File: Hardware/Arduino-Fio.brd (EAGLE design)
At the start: 27.9 x 64.8 mm, 65 parts, among them U1 MCP73831, U4 XBEE, U5 ATMEGA32U4, U6 MIC5219-3.3, X2 USB-MICROB, Y2 8MHz

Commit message: Midway hardware update
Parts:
- X2: value USB-MICROB -> USB_MICROB_PLUGCONN-11752; device SparkFun:USB-MICROB -> SparkFun-Connectors:USB-B-MICRO-SMD_V03
- moved R11 0.32 mm to (7.62, 58.1)
- moved R12 0.32 mm to (8.89, 58.1)
- turned X2 to 270 degrees
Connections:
- removed net N$21: R11.2, X2.D+
- new net N$5: R11.2, X2.D+1
- net GND: now also X2.GND1; no longer X2.GND
- net N$20: now also X2.D-1; no longer X2.D-
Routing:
- net AREF: track 24.8 -> 21.2 mm
- net N$5: track 0.00 -> 1.85 mm
- net N$21: track 1.58 -> 0.00 mm
- net N$1: track 47.2 -> 48.5 mm, vias 1 -> 2
- net GND: track 43.6 -> 42.5 mm, vias 24 -> 27
- net D14: track 47.0 -> 48.1 mm
- net D+: track 43.1 -> 42.4 mm
- net TXO: track 21.9 -> 21.2 mm
- net 3.3V: track 108.5 -> 107.8 mm
- net RST: track 47.4 -> 48.0 mm
- net MOSI: track 38.7 -> 38.2 mm

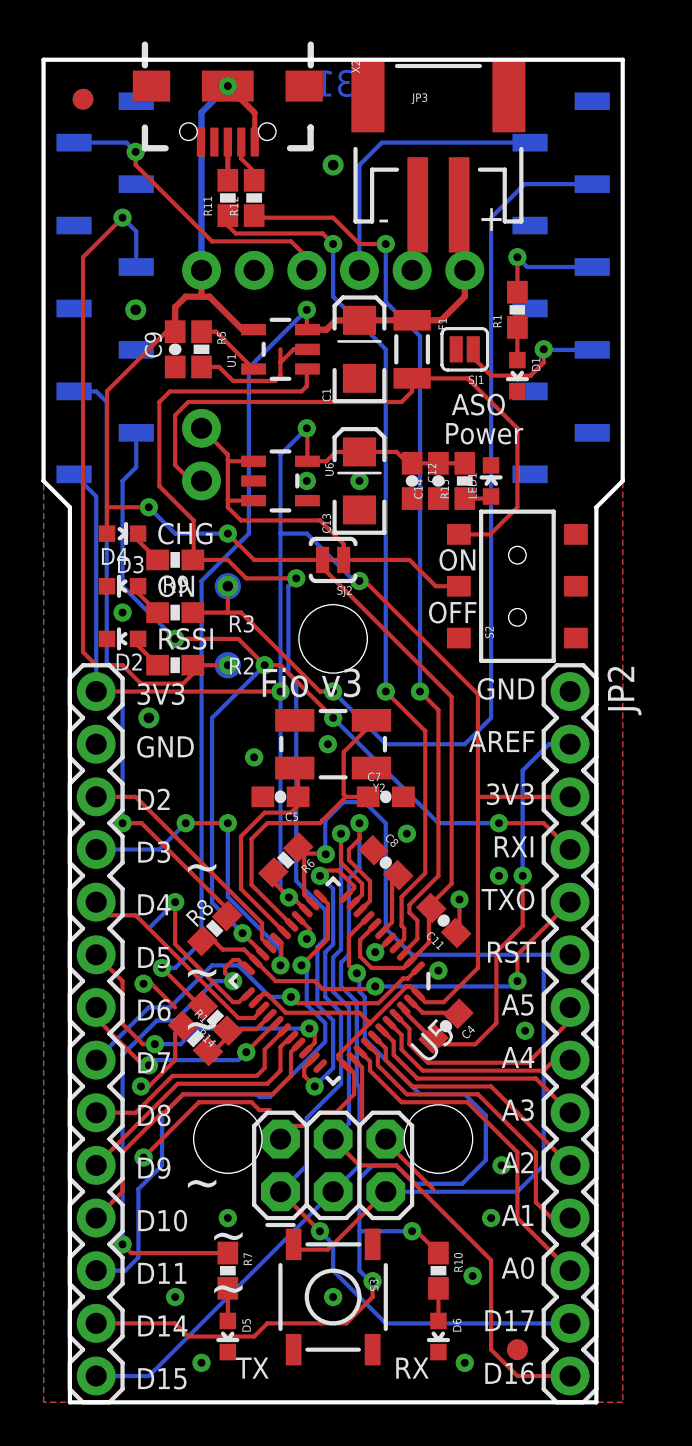
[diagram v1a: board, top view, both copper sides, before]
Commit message: Fixing USB trace issue
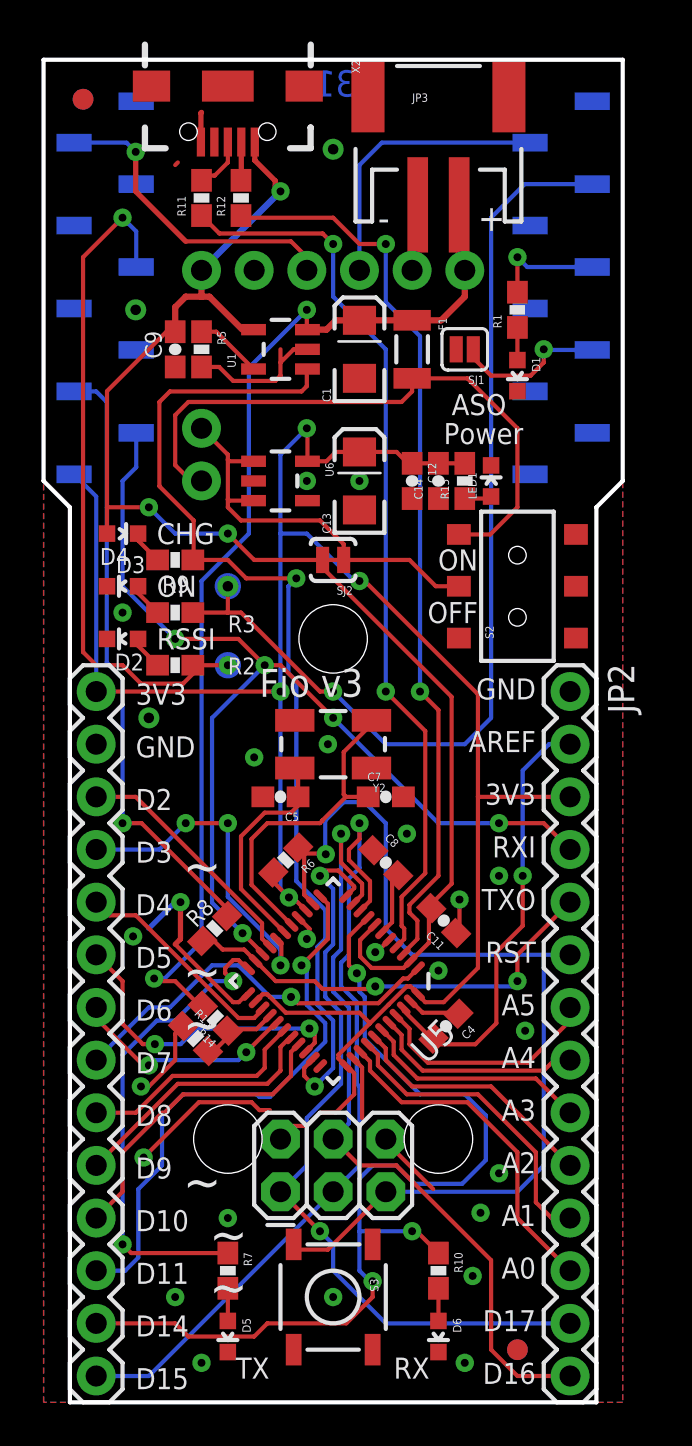
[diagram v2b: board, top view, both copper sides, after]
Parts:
- moved R11 1.27 mm to (6.35, 58.1)
- moved R12 0.63 mm to (8.26, 58.1)
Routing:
- net USB_VCC: track 70.2 -> 65.8 mm
- net D+: track 42.4 -> 43.3 mm
- net N$5: track 1.85 -> 2.61 mm
- net VBATT: track 51.5 -> 52.3 mm
- net SLEEP_RQ: track 14.5 -> 15.3 mm
- net D-: track 43.2 -> 43.9 mm

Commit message: Fixing schematic frame
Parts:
- added U$2: REVISION, SparkFun-Aesthetics:REVISION
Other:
- board text added: "Toni Klopfenstein"
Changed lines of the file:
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@@
 <layer number="47" name="Measures" color="7" fill="1" visible="no" active="yes"/>
 <layer number="48" name="Document" color="7" fill="1" visible="no" active="yes"/>
-<layer number="49" name="Reference" color="7" fill="1" visible="no" active="yes"/>
+<layer number="49" name="Reference" color="7" fill="1" visible="yes" active="yes"/>
 <layer number="50" name="dxf" color="7" fill="1" visible="no" active="yes"/>
 <layer number="51" name="tDocu" color="6" fill="1" visible="yes" active="yes"/>
@@
 <text x="22.479" y="24.765" size="1.016" layer="21" font="vector" ratio="15" rot="R180">TXO</text>
 <text x="22.479" y="22.225" size="1.016" layer="21" font="vector" ratio="15" rot="R180">RST</text>
-<text x="31.75" y="-12.7" size="1.778" layer="27" font="vector" ratio="15">S. Kobayashi and N. Seidle</text>
+<text x="27.94" y="-11.43" size="1.778" layer="27" font="vector" ratio="15">S. Kobayashi and N. Seidle</text>
 <text x="5.715" y="56.261" size="1.27" layer="22" font="vector" ratio="15" rot="MR90">5V</text>
 <text x="9.525" y="55.88" size="1.778" layer="22" font="vector" ratio="15" rot="MR0">-</text>
@@
 <text x="18.034" y="46.228" size="1.016" layer="21" font="vector" ratio="15">Power</text>
 <text x="18.415" y="47.625" size="1.016" layer="21" font="vector" ratio="15">ASO</text>
+<text x="27.94" y="-15.24" size="1.778" layer="27" font="vector" ratio="15">Toni Klopfenstein</text>
 </plain>
 <attributes>
@@
 <element name="FRAME2" library="SparkFun-Aesthetics" package="CREATIVE_COMMONS" value="FRAME-LETTER" x="0.635" y="-11.43"/>
 <element name="LOGO1" library="SparkFun-Aesthetics" package="OSHW-LOGO-L" value="OSHW-LOGOL" x="12.7" y="20.32" rot="MR0"/>
+<element name="U$2" library="SparkFun-Aesthetics" package="REVISION" value="REVISION" x="12.7" y="-15.24"/>
 </elements>
 <signals>
@@
 </signal>
 </signals>
-<errors>
-</errors>
 </board>
 </drawing>

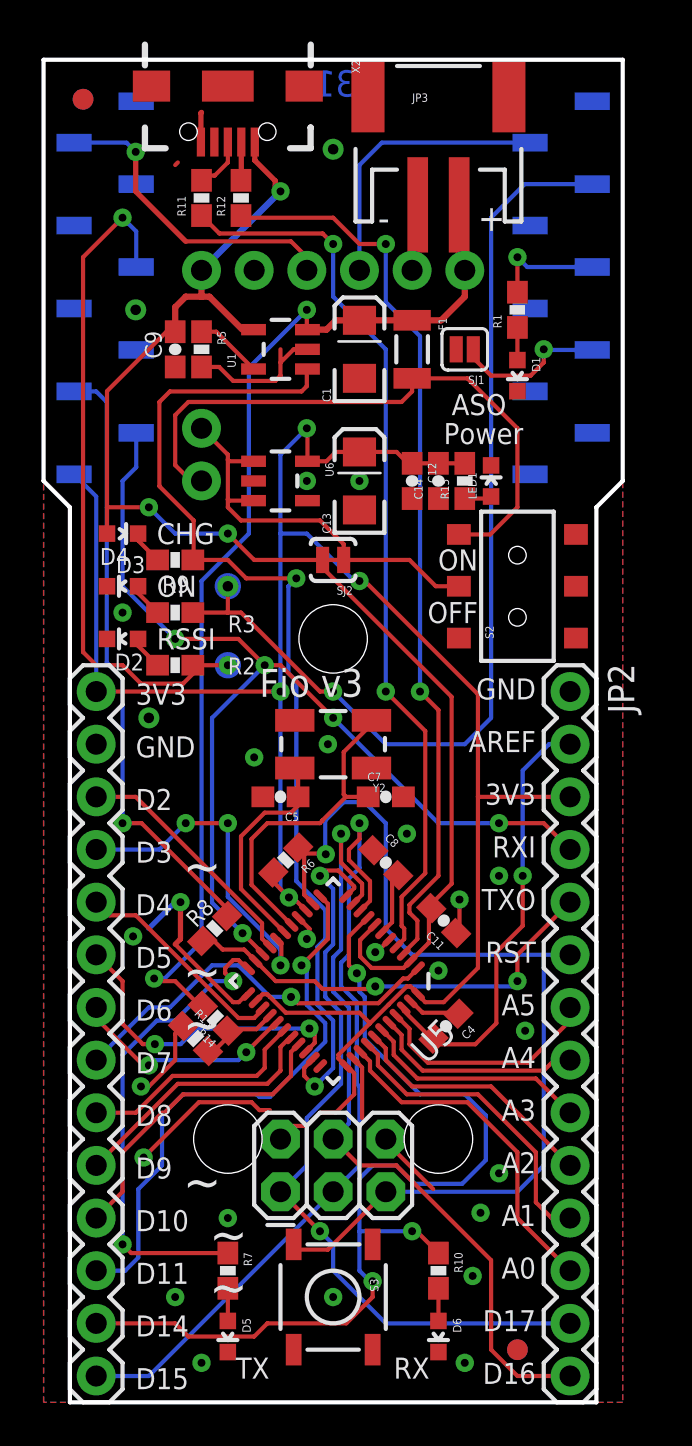
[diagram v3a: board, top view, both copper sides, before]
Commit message: Moved bottom fiducials to clear the Xbee headers
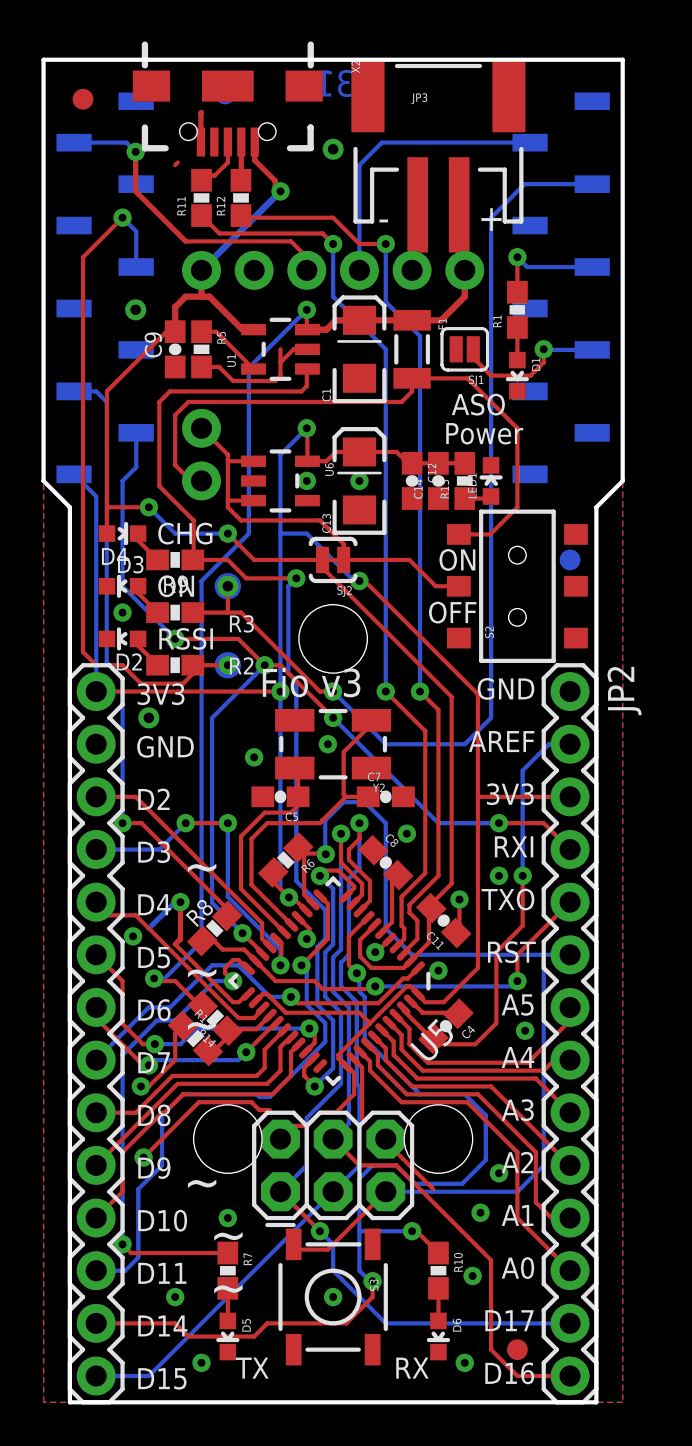
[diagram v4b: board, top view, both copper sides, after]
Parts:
- moved JP13 38.2 mm to (24.1, 40.6)
- moved JP12 6.86 mm to (7.49, 63.1)

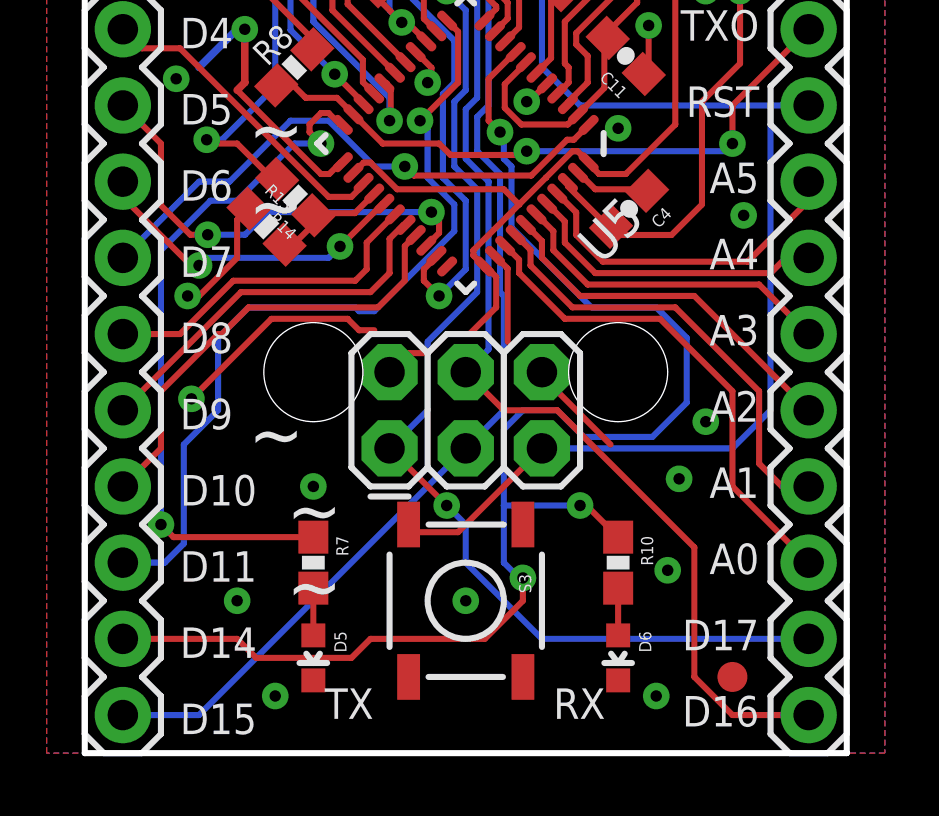
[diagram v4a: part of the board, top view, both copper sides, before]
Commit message: Update Labeling
Updated individual board's silkscreen to correct pins to match the connection to the ATmega32U4 and Arduino core files:

* D17 | RxLED | SS
* D14 | MISO

Replace schematic package to match silkscreen from Brent's fix => [ https://github.com/sparkfun/SparkFun-Eagle-Libraries/issues/77#issuecomment-89820839 ]. Update the net for D17 to match silkscreen.

This should not affect the overall functionality of the board. =P
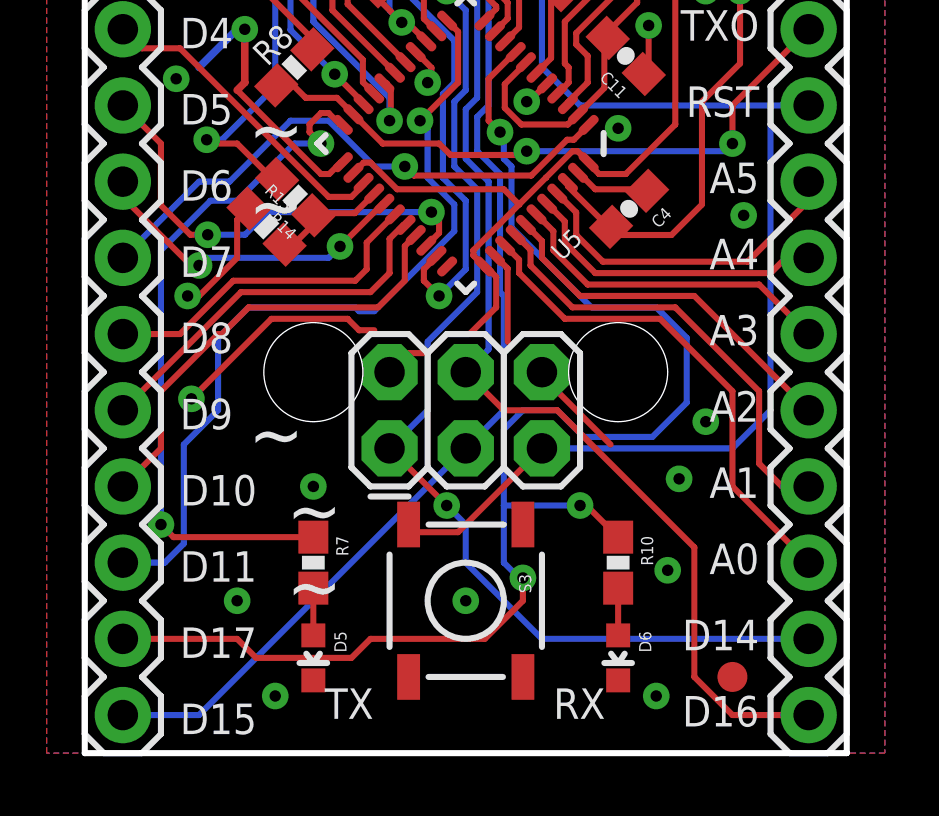
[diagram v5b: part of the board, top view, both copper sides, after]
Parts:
- U5: value ATMEGA32U4 -> ATmega32U4; device Testing:QFN-44-NOPAD_1:1 -> SparkFun-IC-Microcontroller:QFN-44-NOPAD_1:1
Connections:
- net D14 renamed D17
